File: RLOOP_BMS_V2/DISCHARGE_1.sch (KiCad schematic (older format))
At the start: 60 parts, among them Q14 PMV20ENR, Q15 PMV20ENR, Q16 PMV20ENR, Q17 PMV20ENR, Q18 PMV20ENR, Q19 PMV20ENR

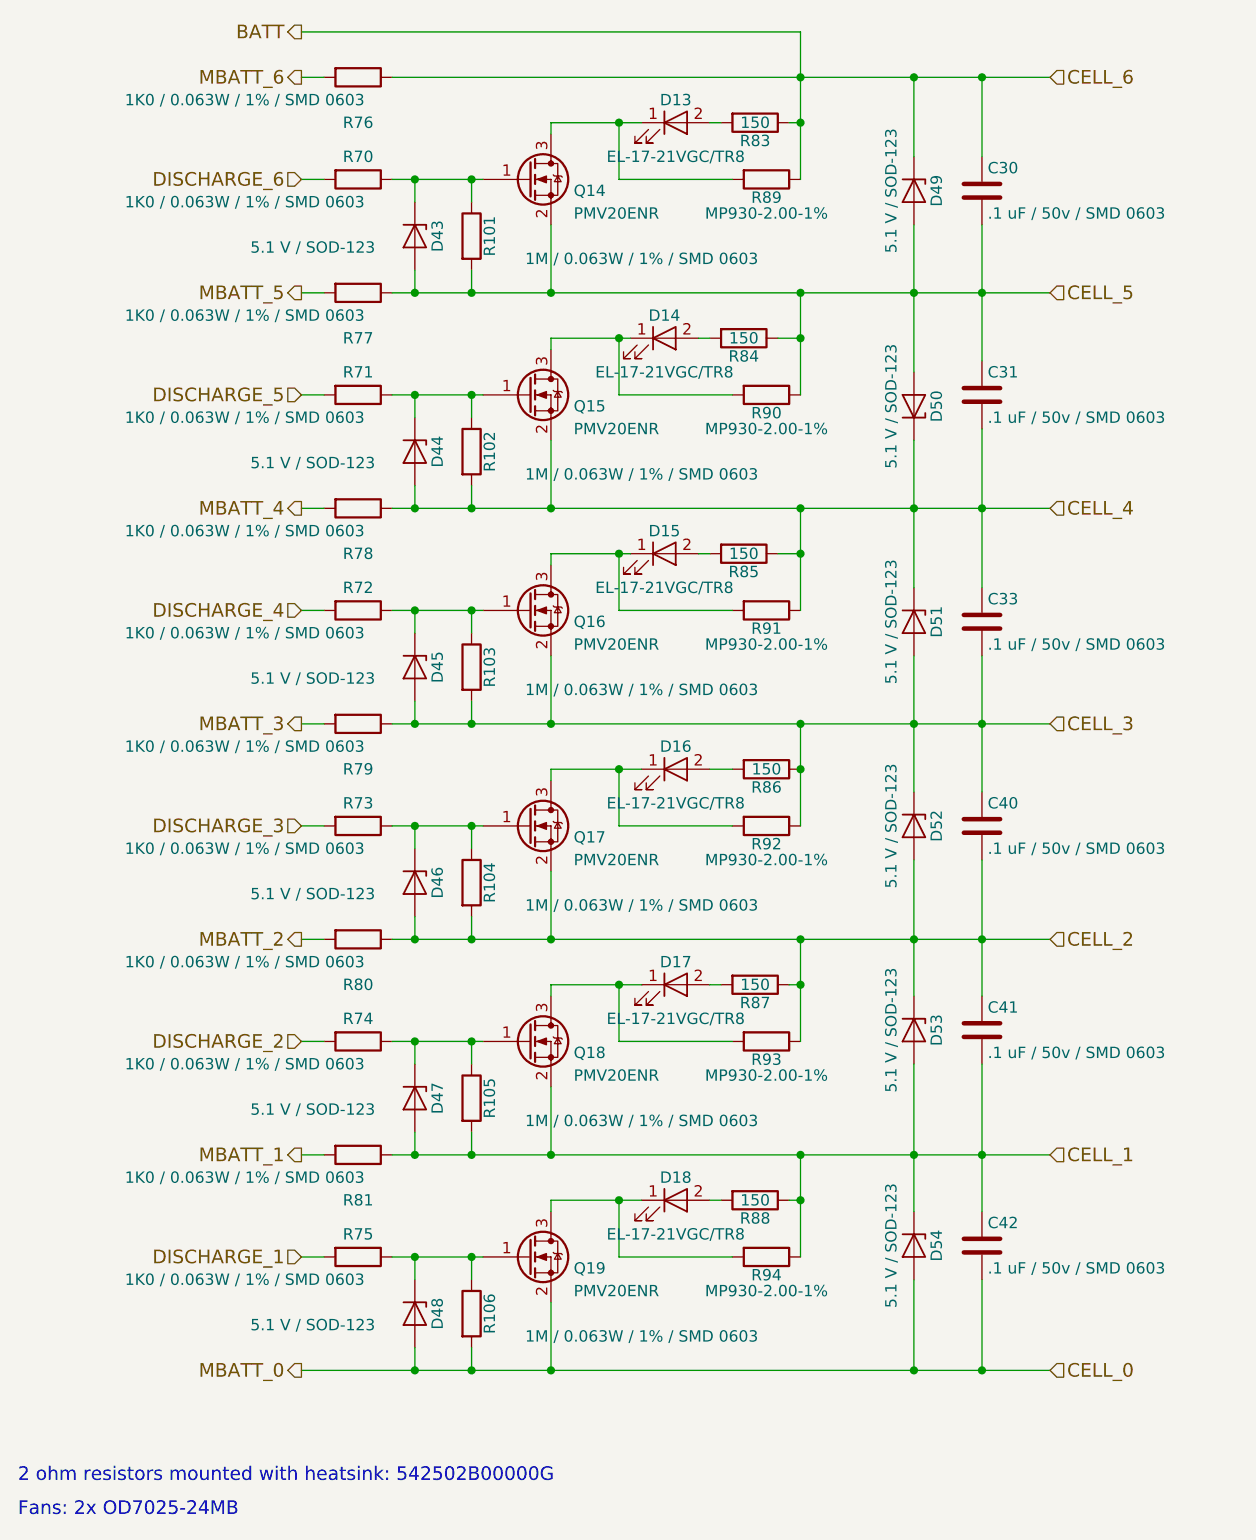
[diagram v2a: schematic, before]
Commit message: Added BOM, added pin 1 markings on a few parts
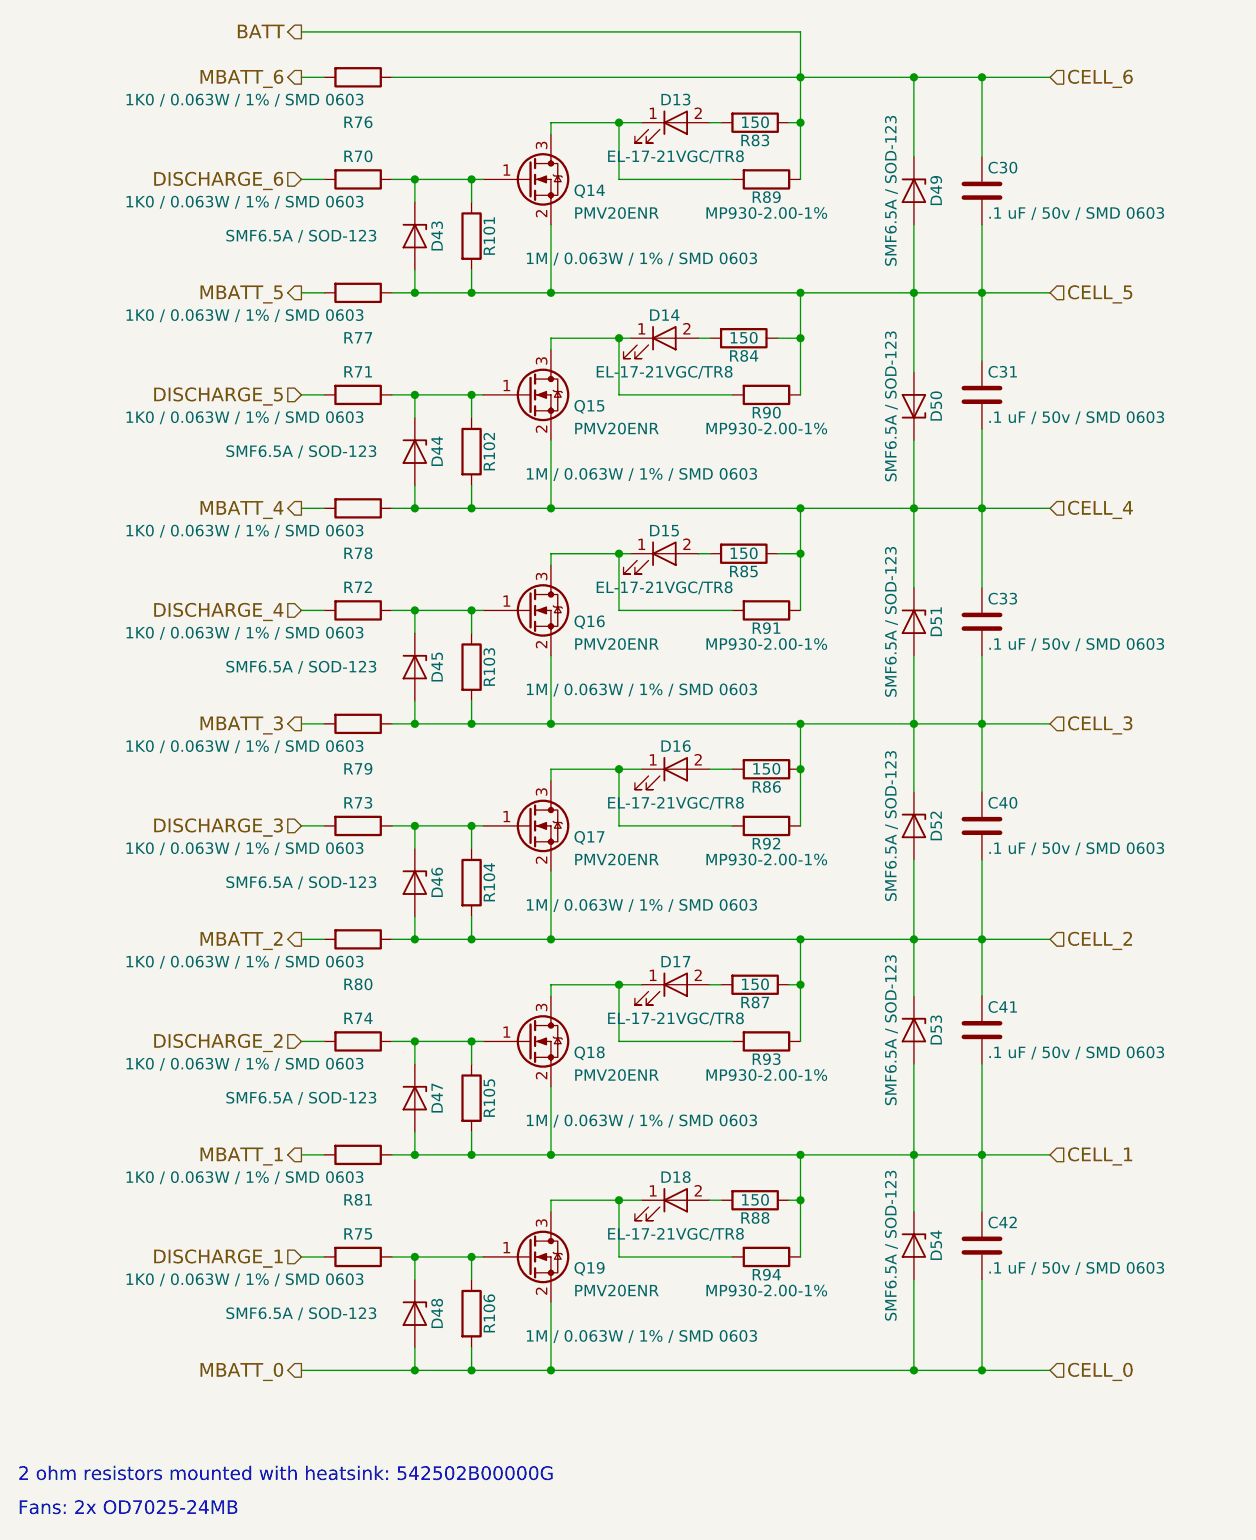
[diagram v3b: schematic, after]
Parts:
- D43, D44, D45, D46, D47, D48, D49, D50, D51, D52, D53, D54: value 5.1 V / SOD-123 -> SMF6.5A / SOD-123
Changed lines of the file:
@@
 P 6050 1300
 F 0 "D49" H 6050 1400 50  0000 C CNN
-F 1 "5.1 V / SOD-123" H 6050 1200 50  0000 C CNN
+F 1 "SMF6.5A / SOD-123" H 6050 1200 50  0000 C CNN
 F 2 "Diodes_SMD:D_SOD-123" H 6050 1300 50  0001 C CNN
 F 3 "" H 6050 1300 50  0001 C CNN
@@
 P 6050 2250
 F 0 "D50" H 6050 2350 50  0000 C CNN
-F 1 "5.1 V / SOD-123" H 6050 2150 50  0000 C CNN
+F 1 "SMF6.5A / SOD-123" H 6050 2150 50  0000 C CNN
 F 2 "Diodes_SMD:D_SOD-123" H 6050 2250 50  0001 C CNN
 F 3 "" H 6050 2250 50  0001 C CNN
@@
 P 6050 3200
 F 0 "D51" H 6050 3300 50  0000 C CNN
-F 1 "5.1 V / SOD-123" H 6050 3100 50  0000 C CNN
+F 1 "SMF6.5A / SOD-123" H 6050 3100 50  0000 C CNN
 F 2 "Diodes_SMD:D_SOD-123" H 6050 3200 50  0001 C CNN
 F 3 "" H 6050 3200 50  0001 C CNN
@@
 P 6050 4100
 F 0 "D52" H 6050 4200 50  0000 C CNN
-F 1 "5.1 V / SOD-123" H 6050 4000 50  0000 C CNN
+F 1 "SMF6.5A / SOD-123" H 6050 4000 50  0000 C CNN
 F 2 "Diodes_SMD:D_SOD-123" H 6050 4100 50  0001 C CNN
 F 3 "" H 6050 4100 50  0001 C CNN
@@
 P 6050 5000
 F 0 "D53" H 6050 5100 50  0000 C CNN
-F 1 "5.1 V / SOD-123" H 6050 4900 50  0000 C CNN
+F 1 "SMF6.5A / SOD-123" H 6050 4900 50  0000 C CNN
 F 2 "Diodes_SMD:D_SOD-123" H 6050 5000 50  0001 C CNN
 F 3 "" H 6050 5000 50  0001 C CNN
@@
 P 6050 5950
 F 0 "D54" H 6050 6050 50  0000 C CNN
-F 1 "5.1 V / SOD-123" H 6050 5850 50  0000 C CNN
+F 1 "SMF6.5A / SOD-123" H 6050 5850 50  0000 C CNN
 F 2 "Diodes_SMD:D_SOD-123" H 6050 5950 50  0001 C CNN
 F 3 "" H 6050 5950 50  0001 C CNN
@@
 P 3850 6250
 F 0 "D48" H 3850 6350 50  0000 C CNN
-F 1 "5.1 V / SOD-123" V 3900 5800 50  0000 C CNN
+F 1 "SMF6.5A / SOD-123" V 3850 5750 50  0000 C CNN
 F 2 "Diodes_SMD:D_SOD-123" H 3850 6250 50  0001 C CNN
 F 3 "" H 3850 6250 50  0001 C CNN
@@
 P 3850 5300
 F 0 "D47" H 3850 5400 50  0000 C CNN
-F 1 "5.1 V / SOD-123" V 3900 4850 50  0000 C CNN
+F 1 "SMF6.5A / SOD-123" V 3850 4800 50  0000 C CNN
 F 2 "Diodes_SMD:D_SOD-123" H 3850 5300 50  0001 C CNN
 F 3 "" H 3850 5300 50  0001 C CNN
@@
 P 3850 4350
 F 0 "D46" H 3850 4450 50  0000 C CNN
-F 1 "5.1 V / SOD-123" V 3900 3900 50  0000 C CNN
+F 1 "SMF6.5A / SOD-123" V 3850 3850 50  0000 C CNN
 F 2 "Diodes_SMD:D_SOD-123" H 3850 4350 50  0001 C CNN
 F 3 "" H 3850 4350 50  0001 C CNN
@@
 P 3850 3400
 F 0 "D45" H 3850 3500 50  0000 C CNN
-F 1 "5.1 V / SOD-123" V 3900 2950 50  0000 C CNN
+F 1 "SMF6.5A / SOD-123" V 3850 2900 50  0000 C CNN
 F 2 "Diodes_SMD:D_SOD-123" H 3850 3400 50  0001 C CNN
 F 3 "" H 3850 3400 50  0001 C CNN
@@
 P 3850 2450
 F 0 "D44" H 3850 2550 50  0000 C CNN
-F 1 "5.1 V / SOD-123" V 3900 2000 50  0000 C CNN
+F 1 "SMF6.5A / SOD-123" V 3850 1950 50  0000 C CNN
 F 2 "Diodes_SMD:D_SOD-123" H 3850 2450 50  0001 C CNN
 F 3 "" H 3850 2450 50  0001 C CNN
@@
 P 3850 1500
 F 0 "D43" H 3850 1600 50  0000 C CNN
-F 1 "5.1 V / SOD-123" V 3900 1050 50  0000 C CNN
+F 1 "SMF6.5A / SOD-123" V 3850 1000 50  0000 C CNN
 F 2 "Diodes_SMD:D_SOD-123" H 3850 1500 50  0001 C CNN
 F 3 "" H 3850 1500 50  0001 C CNN

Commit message: Change 2 Ohm Resistor
Had to change for heatsink mounting :/
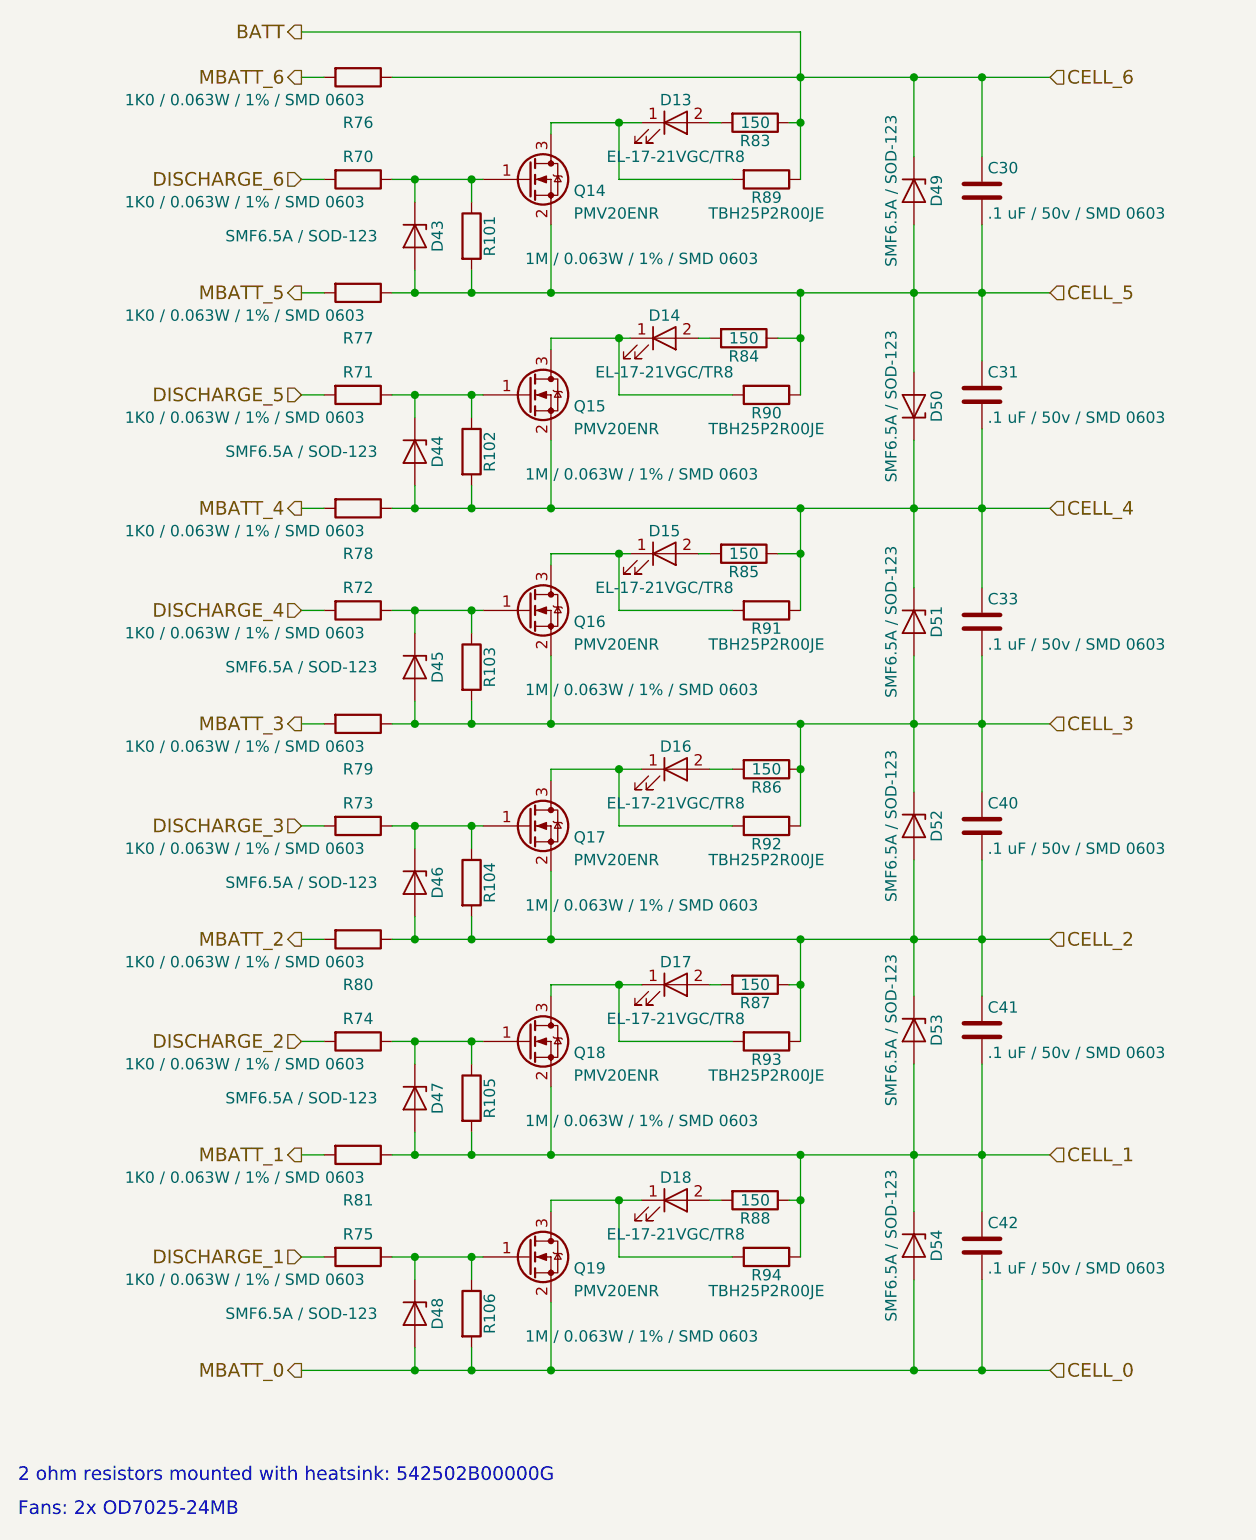
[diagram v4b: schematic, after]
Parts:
- R89, R90, R91, R92, R93, R94: value MP930-2.00-1% -> TBH25P2R00JE
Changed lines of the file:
@@
 P 5400 1250
 F 0 "R89" V 5480 1250 50  0000 C CNN
-F 1 "MP930-2.00-1%" V 5550 1250 50  0000 C CNN
+F 1 "TBH25P2R00JE" V 5550 1250 50  0000 C CNN
 F 2 "rLoop_Footprints:Res_MP930" V 5330 1250 50  0001 C CNN
 F 3 "" H 5400 1250 50  0001 C CNN
@@
 P 5400 2200
 F 0 "R90" V 5480 2200 50  0000 C CNN
-F 1 "MP930-2.00-1%" V 5550 2200 50  0000 C CNN
+F 1 "TBH25P2R00JE" V 5550 2200 50  0000 C CNN
 F 2 "rLoop_Footprints:Res_MP930" V 5330 2200 50  0001 C CNN
 F 3 "" H 5400 2200 50  0001 C CNN
@@
 P 5400 3150
 F 0 "R91" V 5480 3150 50  0000 C CNN
-F 1 "MP930-2.00-1%" V 5550 3150 50  0000 C CNN
+F 1 "TBH25P2R00JE" V 5550 3150 50  0000 C CNN
 F 2 "rLoop_Footprints:Res_MP930" V 5330 3150 50  0001 C CNN
 F 3 "" H 5400 3150 50  0001 C CNN
@@
 P 5400 4100
 F 0 "R92" V 5480 4100 50  0000 C CNN
-F 1 "MP930-2.00-1%" V 5550 4100 50  0000 C CNN
+F 1 "TBH25P2R00JE" V 5550 4100 50  0000 C CNN
 F 2 "rLoop_Footprints:Res_MP930" V 5330 4100 50  0001 C CNN
 F 3 "" H 5400 4100 50  0001 C CNN
@@
 P 5400 5050
 F 0 "R93" V 5480 5050 50  0000 C CNN
-F 1 "MP930-2.00-1%" V 5550 5050 50  0000 C CNN
+F 1 "TBH25P2R00JE" V 5550 5050 50  0000 C CNN
 F 2 "rLoop_Footprints:Res_MP930" V 5330 5050 50  0001 C CNN
 F 3 "" H 5400 5050 50  0001 C CNN
@@
 P 5400 6000
 F 0 "R94" V 5480 6000 50  0000 C CNN
-F 1 "MP930-2.00-1%" V 5550 6000 50  0000 C CNN
+F 1 "TBH25P2R00JE" V 5550 6000 50  0000 C CNN
 F 2 "rLoop_Footprints:Res_MP930" V 5330 6000 50  0001 C CNN
 F 3 "" H 5400 6000 50  0001 C CNN

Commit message: swapped a few connectors to standardize with the power node and what's readily available
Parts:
- R89, R90, R91, R92, R93, R94: footprint rLoop_Footprints:Res_MP930 -> rLoop_Footprints:2-OHM-TO-220-TBH25P2R00JE
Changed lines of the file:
@@
 F 0 "R89" V 5480 1250 50  0000 C CNN
 F 1 "TBH25P2R00JE" V 5550 1250 50  0000 C CNN
-F 2 "rLoop_Footprints:Res_MP930" V 5330 1250 50  0001 C CNN
+F 2 "rLoop_Footprints:2-OHM-TO-220-TBH25P2R00JE" V 5330 1250 50  0001 C CNN
 F 3 "" H 5400 1250 50  0001 C CNN
 	1    5400 1250
@@
 F 0 "R90" V 5480 2200 50  0000 C CNN
 F 1 "TBH25P2R00JE" V 5550 2200 50  0000 C CNN
-F 2 "rLoop_Footprints:Res_MP930" V 5330 2200 50  0001 C CNN
+F 2 "rLoop_Footprints:2-OHM-TO-220-TBH25P2R00JE" V 5330 2200 50  0001 C CNN
 F 3 "" H 5400 2200 50  0001 C CNN
 	1    5400 2200
@@
 F 0 "R91" V 5480 3150 50  0000 C CNN
 F 1 "TBH25P2R00JE" V 5550 3150 50  0000 C CNN
-F 2 "rLoop_Footprints:Res_MP930" V 5330 3150 50  0001 C CNN
+F 2 "rLoop_Footprints:2-OHM-TO-220-TBH25P2R00JE" V 5330 3150 50  0001 C CNN
 F 3 "" H 5400 3150 50  0001 C CNN
 	1    5400 3150
@@
 F 0 "R92" V 5480 4100 50  0000 C CNN
 F 1 "TBH25P2R00JE" V 5550 4100 50  0000 C CNN
-F 2 "rLoop_Footprints:Res_MP930" V 5330 4100 50  0001 C CNN
+F 2 "rLoop_Footprints:2-OHM-TO-220-TBH25P2R00JE" V 5330 4100 50  0001 C CNN
 F 3 "" H 5400 4100 50  0001 C CNN
 	1    5400 4100
@@
 F 0 "R93" V 5480 5050 50  0000 C CNN
 F 1 "TBH25P2R00JE" V 5550 5050 50  0000 C CNN
-F 2 "rLoop_Footprints:Res_MP930" V 5330 5050 50  0001 C CNN
+F 2 "rLoop_Footprints:2-OHM-TO-220-TBH25P2R00JE" V 5330 5050 50  0001 C CNN
 F 3 "" H 5400 5050 50  0001 C CNN
 	1    5400 5050
@@
 F 0 "R94" V 5480 6000 50  0000 C CNN
 F 1 "TBH25P2R00JE" V 5550 6000 50  0000 C CNN
-F 2 "rLoop_Footprints:Res_MP930" V 5330 6000 50  0001 C CNN
+F 2 "rLoop_Footprints:2-OHM-TO-220-TBH25P2R00JE" V 5330 6000 50  0001 C CNN
 F 3 "" H 5400 6000 50  0001 C CNN
 	1    5400 6000
